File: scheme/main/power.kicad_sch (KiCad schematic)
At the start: 36 parts, among them U15 SCWN06B-15, U16 K7809-1000R3, U17 K7803-1000R3, U18 LD1117S50TR_SOT223, U19 IFX1117MEV33HTMA1, U20 K7805-1000R3

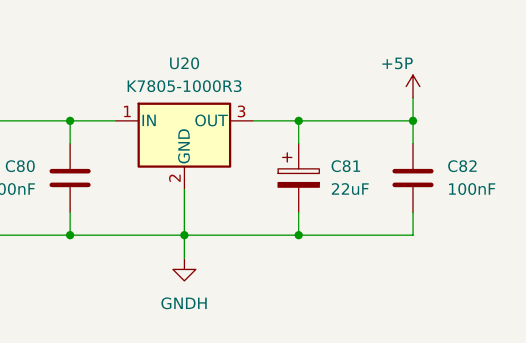
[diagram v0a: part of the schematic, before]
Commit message: added analog input 0 && sheets sort
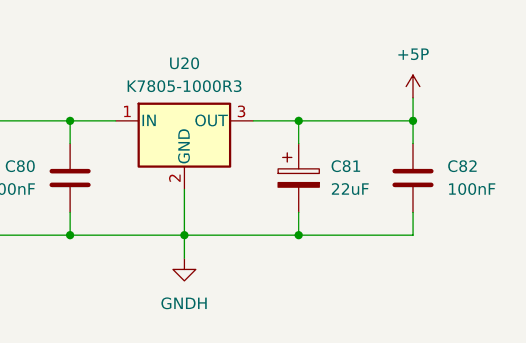
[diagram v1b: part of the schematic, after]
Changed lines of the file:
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@@
 		(shape input)
 		(at 38.1 35.56 180)
-		(fields_autoplaced yes)
 		(effects
 			(font
@@
 		(shape input)
 		(at 38.1 40.64 180)
-		(fields_autoplaced yes)
 		(effects
 			(font
@@
 		(shape input)
 		(at 45.72 85.09 180)
-		(fields_autoplaced yes)
 		(effects
 			(font
@@
 		)
 		(property "Value" "+5P"
-			(at 259.842 24.13 0)
+			(at 261.62 23.114 0)
 			(effects
 				(font
